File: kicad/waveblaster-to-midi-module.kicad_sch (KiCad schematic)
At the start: 14 parts, among them J1 Midi Out, J2 Midi In, J3 Right In, J4 Left In, J5 Right Out, J6 Left Out, J7 Wavetable Input, U1 H11L1

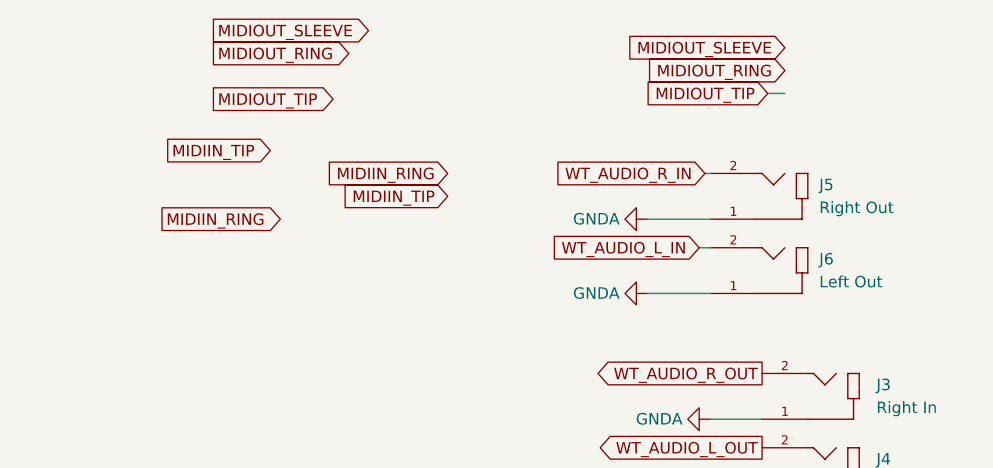
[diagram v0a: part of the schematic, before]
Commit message: v2.0: low profile
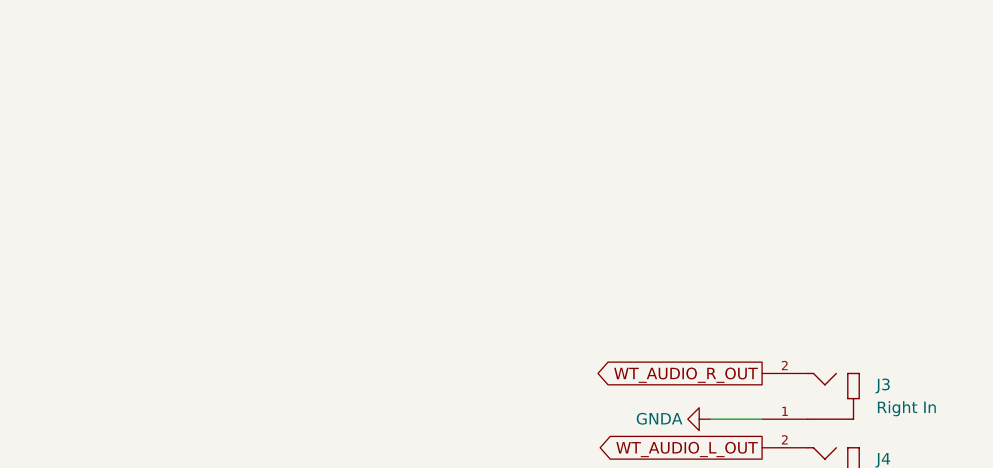
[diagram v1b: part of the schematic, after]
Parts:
- removed J5: Right Out, Library:CUI_RCJ-04X, symbol RCJ-04X:RCJ-043
- removed J6: Left Out, Library:CUI_RCJ-043, symbol RCJ-04X:RCJ-043
